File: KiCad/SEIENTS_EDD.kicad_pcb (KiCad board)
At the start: 2 copper layers, 144.1 x 110 mm, 99 parts, among them IC1 A3144EUA, J1 Conn_01x02_Pin, J201 Screw_Terminal_01x04, J3 Screw_Terminal_01x05, J4 Screw_Terminal_01x02, J7 DE9_Socket, J8 DE9_Pins, M4 Motor_DC, M5 Motor_DC, M6 Motor_DC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

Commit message: Routing V1
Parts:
- U4: footprint Package_TO_SOT_SMD:SOT-563 -> MICRO:SOT-563
- moved C304 61.0 mm to (82.7, 50.1), turned to 180 degrees
- moved C302 54.1 mm to (82.7, 55.1), turned to 180 degrees
- moved TP2 38.2 mm to (118.3, 34.0)
- moved R14 21.6 mm to (121.3, 109.5), turned to 90 degrees
- moved TP10 17.8 mm to (137.4, 82.5)
- moved C14 13.9 mm to (143.6, 77.2), turned to 90 degrees
- moved C11 13.0 mm to (148.4, 77.3), turned to 90 degrees
- moved R100 6.66 mm to (126.4, 88.4)
- moved IC1 5.25 mm to (115.7, 72.5), turned to 180 degrees
- moved R209 4.37 mm to (141.0, 111.1)
- moved R23 3.57 mm to (127.7, 68.9), turned to 180 degrees
- moved R26 1.98 mm to (120.6, 112.2)
- moved C12 1.97 mm to (191.1, 37.3)
- moved R210 1.83 mm to (115.5, 120.0), turned to 180 degrees
- moved TP4 1.74 mm to (172.7, 32.6)
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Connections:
- J201 pad 2: VBAT -> unconnected-(J201-Pin_2-Pad2)
- J7 pad 9: +5V -> unconnected-(J7-Pad9)
- J8 pad 6: +5V -> unconnected-(J8-Pad6)
- U5 pad 21: POS_IN1 -> POS_IN2
- U5 pad 22: POS_IN2 -> POS_IN1
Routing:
- net GND: track 0.00 -> 171.1 mm, vias 0 -> 128
- net MCU_SDA: track 0.00 -> 72.8 mm
- net VBAT: track 0.00 -> 70.2 mm
- net MCU_SCL: track 0.00 -> 69.6 mm
- net CINTO: track 0.00 -> 64.4 mm, vias 0 -> 3
- net +5V: track 0.00 -> 57.5 mm
- net Net-(M4--): track 0.00 -> 43.9 mm
- net HALL_OUT: track 0.00 -> 41.9 mm, vias 0 -> 1
- net Net-(M4-+): track 0.00 -> 41.7 mm, vias 0 -> 1
- net Net-(J201-Pin_1): track 0.00 -> 36.7 mm, vias 0 -> 2
- net CALEFACCIÓ: track 0.00 -> 35.9 mm
- net Net-(D2-A): track 0.00 -> 35.7 mm
- net Net-(M5--): track 0.00 -> 34.9 mm
- net Net-(C72-Pad1): track 0.00 -> 34.7 mm
- net Net-(D1-A1): track 0.00 -> 32.6 mm
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- added copper zone on F.Cu, net +3.3V
- added copper zone on F.Cu, net +5V
- added copper zone on B.Cu, net GND

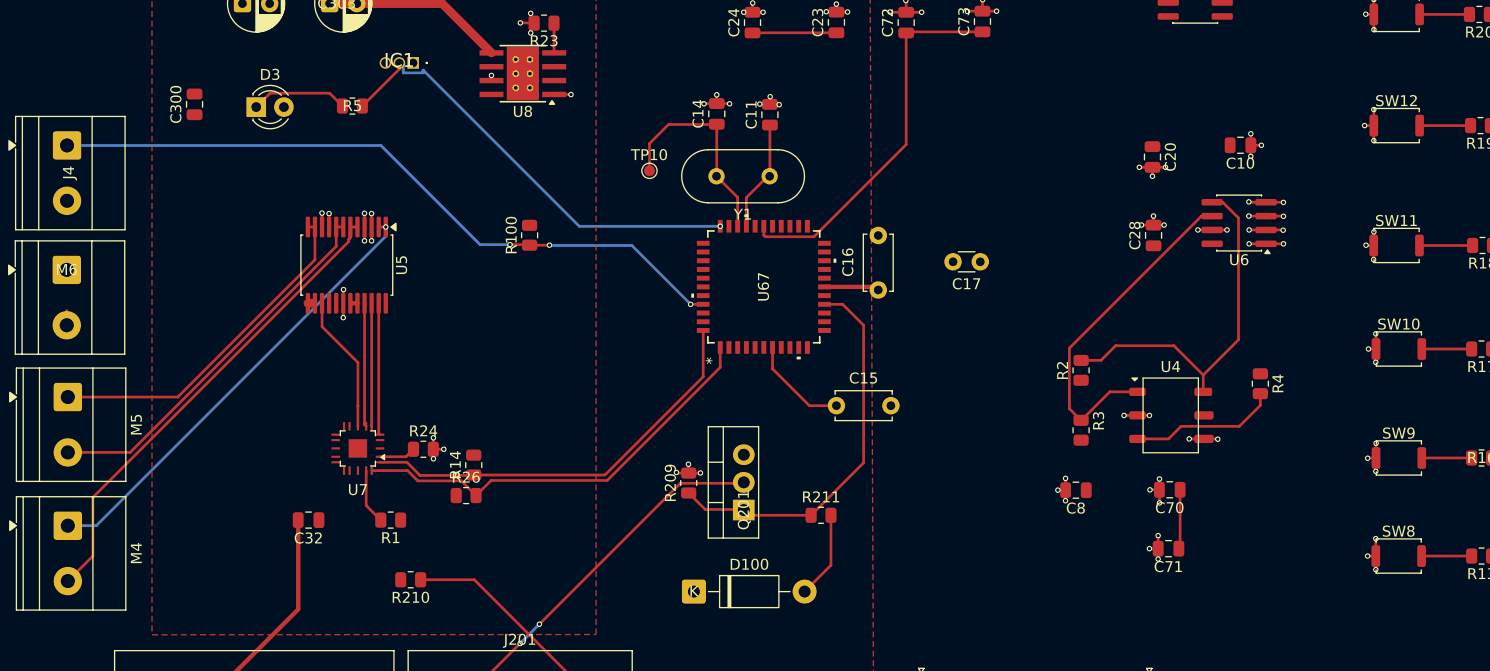
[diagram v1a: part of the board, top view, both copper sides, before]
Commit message: Modificació al routing
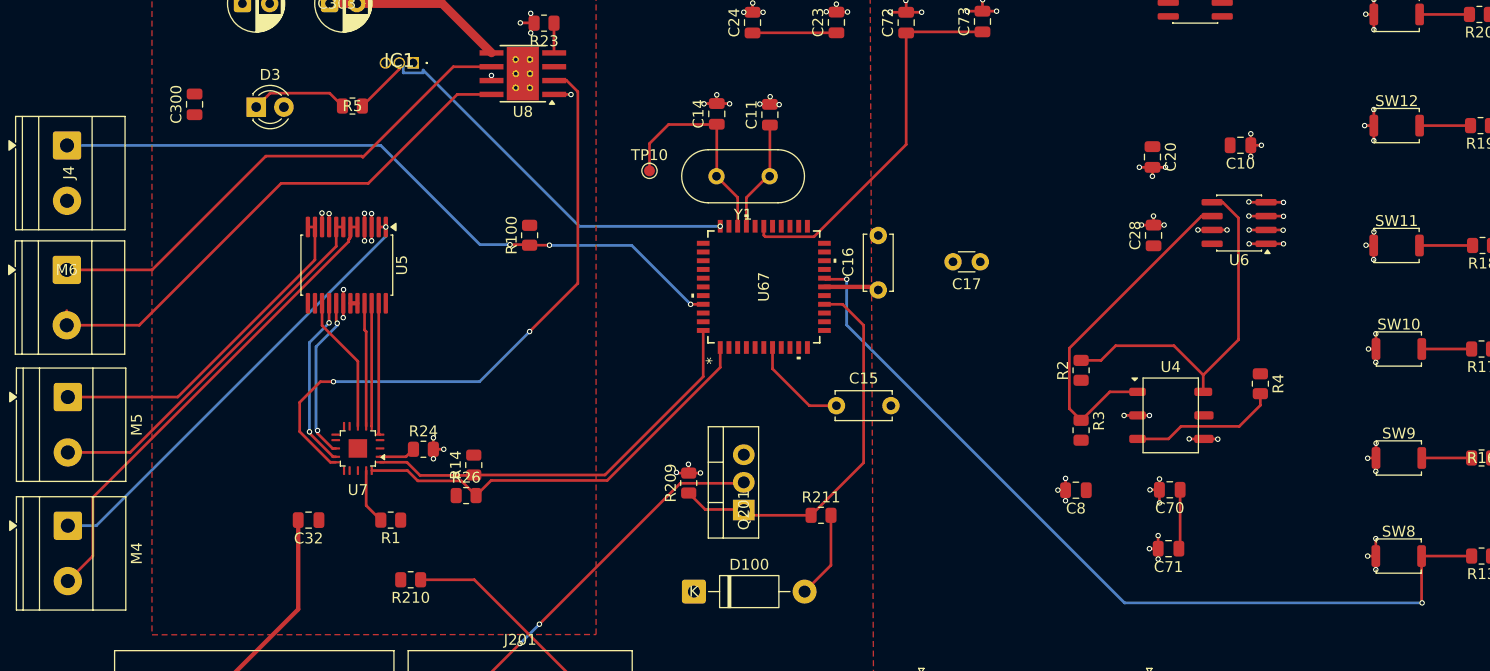
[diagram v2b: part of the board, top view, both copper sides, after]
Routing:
- net Net-(J3-Pin_1): track 4.59 -> 78.6 mm, vias 0 -> 2
- net ALT_IN2: track 0.00 -> 57.4 mm, vias 0 -> 2
- net Net-(M6--): track 1.35 -> 49.1 mm
- net Net-(M6-+): track 0.00 -> 46.8 mm
- net REC_IN2: track 0.00 -> 16.0 mm, vias 0 -> 2
- net REC_IN1: track 0.00 -> 15.1 mm, vias 0 -> 2

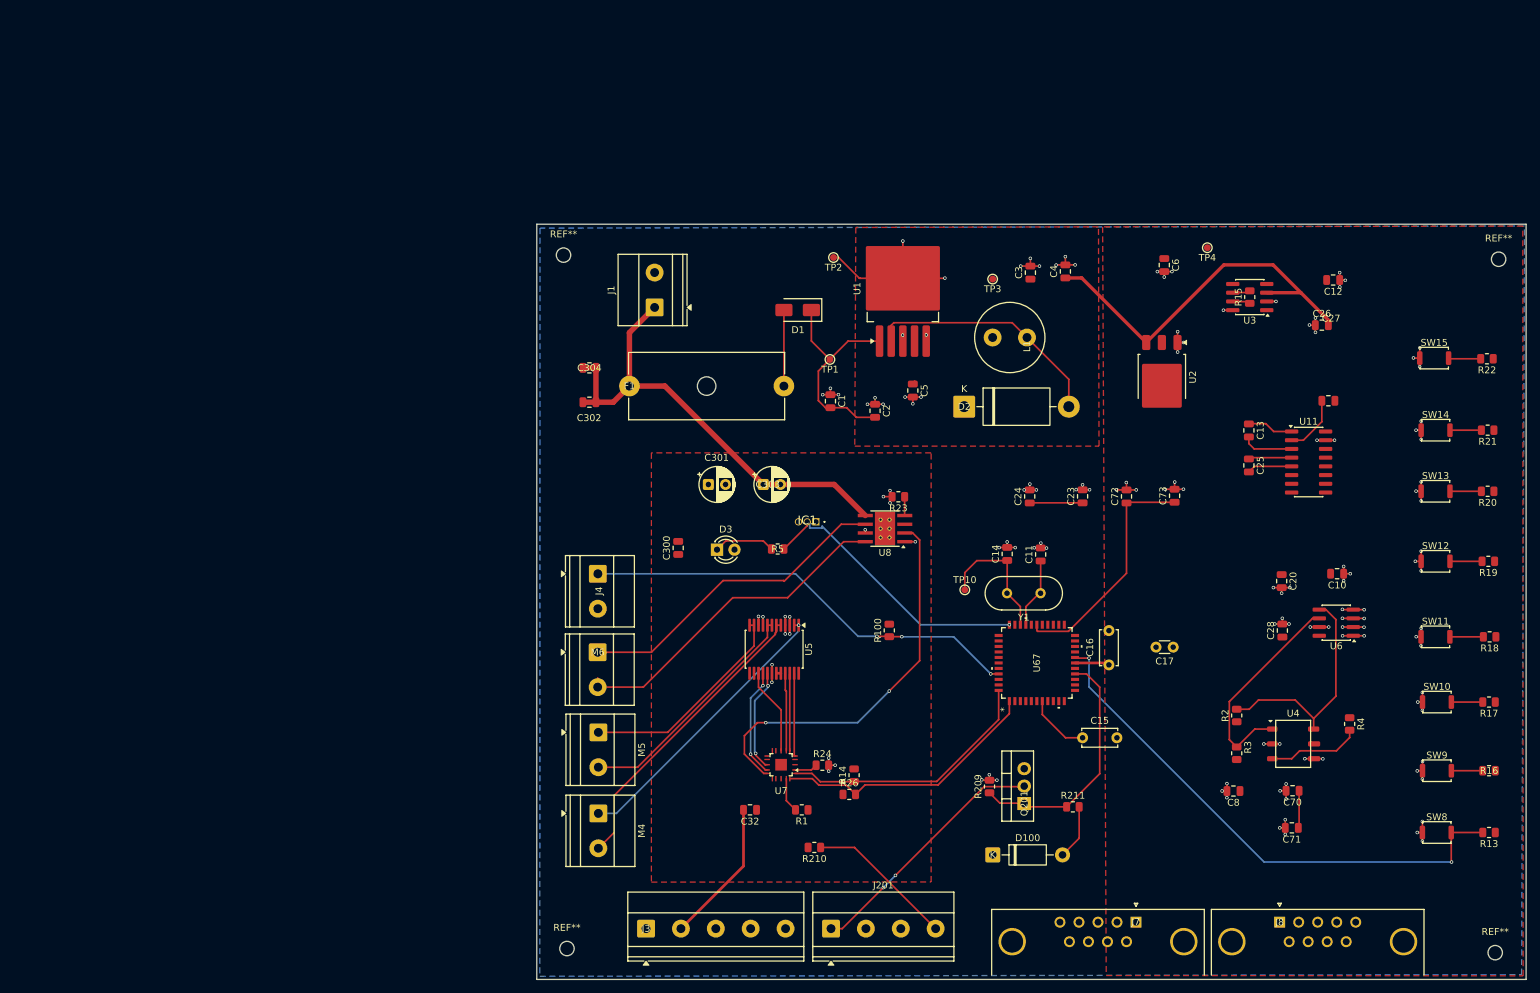
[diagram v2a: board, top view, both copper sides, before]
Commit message: Modificació al routing
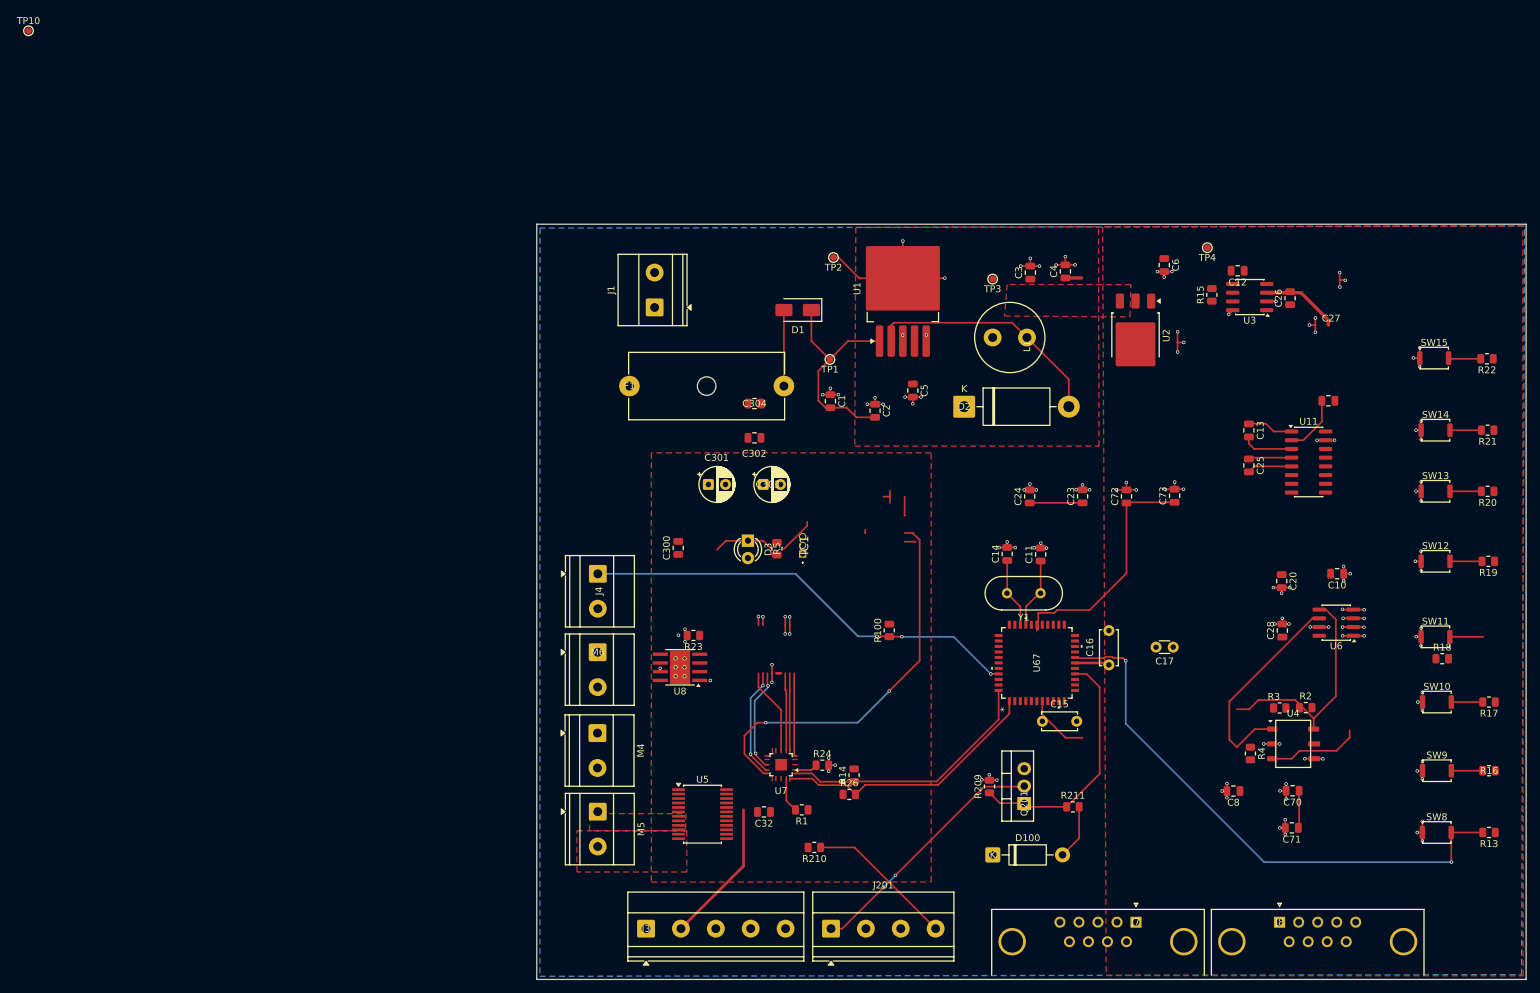
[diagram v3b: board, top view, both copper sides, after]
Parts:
- removed REF** (x4): MountingHole_2.1mm, MountingHole:MountingHole_2.1mm
- moved TP10 158.8 mm to (1.02, 1.02)
- moved U8 36.0 mm to (95.9, 93.7)
- moved R23 36.0 mm to (97.9, 89.1)
- moved U5 26.2 mm to (99.2, 115.1), turned to 0 degrees
- moved C302 24.6 mm to (106.8, 60.3)
- moved C304 24.6 mm to (106.8, 55.3)
- moved R4 15.1 mm to (179.0, 106.3)
- moved C12 14.0 mm to (177.1, 36.0)
- moved M4 11.7 mm to (83.9, 103.3)
- moved M5 11.6 mm to (83.9, 114.8)
- moved R2 10.1 mm to (187.1, 99.6), turned to 0 degrees
- moved R3 9.10 mm to (183.3, 99.7), turned to 180 degrees
- moved R18 7.60 mm to (206.9, 92.5), turned to 0 degrees
- moved U2 7.16 mm to (162.3, 45.4)
- moved C15 6.33 mm to (148.7, 101.6)
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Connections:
- C300 pad 2: +3.3V -> Net-(C300-Pad2)
- C301 pad 2: +3.3V -> Net-(C300-Pad2)
- C302 pad 1: VBAT -> VBAT/FUSE
- C302 pad 2: VBAT -> GND
- C303 pad 1: VBAT -> VBAT/FUSE
- C303 pad 2: VBAT -> GND
- C304 pad 2: VBAT -> GND
- C32 pad 2: +3.3V -> GND
- D1 pad 2: Net-(D1-A2) -> VBAT/FUSE
- F1 pad 2: Net-(D1-A2) -> VBAT/FUSE
- U5 pad 11: Net-(M5-+) -> Net-(M5--)
- U5 pad 12: Net-(M5-+) -> Net-(M5--)
- U5 pad 13: VBAT -> VBAT/FUSE
- U5 pad 14: VBAT -> VBAT/FUSE
- U5 pad 24: VBAT -> VBAT/FUSE
- U5 pad 7: Net-(M5--) -> Net-(M5-+)
- U5 pad 8: Net-(M5--) -> Net-(M5-+)
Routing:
- net VBAT: track 69.8 -> 0.00 mm
- net Net-(M6--): track 49.1 -> 0.00 mm
- net Net-(M6-+): track 46.8 -> 0.00 mm
- net Net-(M4--): track 43.9 -> 0.00 mm
- net +5V: track 57.5 -> 15.3 mm
- net HALL_OUT: track 41.9 -> 0.00 mm, vias 1 -> 0
- net Net-(M4-+): track 41.7 -> 0.00 mm, vias 1 -> 0
- net Net-(M5--): track 34.9 -> 0.00 mm
- net Net-(M5-+): track 31.6 -> 0.00 mm
- net VBAT/FUSE: track 0.00 -> 11.1 mm
- net Net-(D1-A2): track 11.1 -> 0.00 mm
- net Net-(U67-OSC2/CLKO/CN29/RA3): track 19.6 -> 10.2 mm
- net GND: track 171.1 -> 175.9 mm
- net Net-(J3-Pin_1): track 78.6 -> 81.6 mm
- net CANL: track 2.59 -> 0.04 mm
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- added copper zone on F.Cu, net Net-(M5-+)
- added copper zone on F.Cu, net Net-(M5--)

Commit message: Routing V2
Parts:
- added REF**: MountingHole_3mm, MountingHole:MountingHole_3mm, F.Cu at (79.2, 33.6)
- added REF**: MountingHole_3mm, MountingHole:MountingHole_3mm, F.Cu at (214.6, 134.6)
- added REF**: MountingHole_3mm, MountingHole:MountingHole_3mm, F.Cu at (214.1, 33.8)
- added REF**: MountingHole_3mm, MountingHole:MountingHole_3mm, F.Cu at (79.8, 134.5)
- moved R18 7.76 mm to (214.0, 89.3), turned to 180 degrees
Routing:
- net ALT_IN2: track 57.4 -> 0.50 mm, vias 2 -> 0
- net GND: track 175.9 -> 145.8 mm, vias 128 -> 111
- net +3.3V: track 26.8 -> 5.06 mm
- net REC_IN2: track 16.0 -> 0.24 mm, vias 2 -> 0
- net REC_IN1: track 15.1 -> 0.29 mm, vias 2 -> 0
- net +5V: track 15.3 -> 1.58 mm
- net Net-(U4-ALERT): track 13.6 -> 0.00 mm
- net REC_PWM: track 12.6 -> 0.00 mm
- net POS_PWM: track 12.1 -> 0.17 mm
- net POS_IN2: track 11.3 -> 0.00 mm
- net POS_IN1: track 11.3 -> 0.01 mm
- net Net-(D3-K): track 8.93 -> 0.00 mm
- net Net-(U8-ILIM): track 2.74 -> 0.00 mm
- added copper zone on B.Cu, net +3.3V
- added copper zone on B.Cu, net +5V
- added copper zone on F.Cu, net GND
- removed copper zone on F.Cu, net +3.3V
- removed copper zone on B.Cu, net GND

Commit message: Modificació al routing
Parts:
- removed REF** (x4): MountingHole_3mm, MountingHole:MountingHole_3mm
- removed TP10: TestPoint, TestPoint:TestPoint_Pad_D1.0mm
- C16: footprint Capacitor_THT:C_Disc_D5.0mm_W2.5mm_P5.00mm -> Capacitor_SMD:C_0805_2012Metric
- moved R15 84.7 mm to (147.9, 120.3)
- moved U3 84.7 mm to (153.4, 120.6)
- moved C26 84.4 mm to (161.0, 121.0)
- moved C12 82.4 mm to (155.6, 115.5)
- moved J3 78.5 mm to (148.6, 78.5), turned to -90 degrees
- moved R209 56.6 mm to (87.8, 130.2), turned to -90 degrees
- moved Q201 54.5 mm to (93.9, 129.3), turned to -90 degrees
- moved C8 35.1 mm to (142.6, 120.8), turned to -90 degrees
- moved R100 32.0 mm to (95.7, 79.2)
- moved Y1 27.6 mm to (124.8, 68.8)
- moved C11 27.6 mm to (124.8, 63.1)
- moved C14 27.6 mm to (119.9, 63.1)
- moved C17 27.0 mm to (149.2, 71.2), turned to 90 degrees
- moved C16 26.7 mm to (145.4, 70.0)
- moved SW15 23.3 mm to (224.7, 35.1)
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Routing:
- net +3.3V: track 5.06 -> 319.9 mm, vias 0 -> 4
- net RX: track 0.00 -> 99.7 mm, vias 0 -> 2
- net TX: track 0.00 -> 99.5 mm, vias 0 -> 2
- net MCU_SDA: track 72.8 -> 0.00 mm
- net MCU_SCL: track 69.6 -> 0.00 mm
- net Net-(J3-Pin_1): track 81.6 -> 15.7 mm, vias 2 -> 0
- net +5V: track 1.58 -> 60.5 mm, vias 0 -> 2
- net CALEFACCIÓ: track 35.9 -> 83.1 mm
- net ALT_IN1: track 0.00 -> 36.1 mm, vias 0 -> 2
- net CANH: track 0.04 -> 34.5 mm
- net CANL: track 0.04 -> 31.7 mm
- net Net-(M4-+): track 0.00 -> 30.7 mm
- net Net-(J201-Pin_1): track 36.7 -> 7.71 mm, vias 2 -> 0
- net Net-(M4--): track 0.00 -> 28.6 mm
- net GND: track 145.8 -> 167.7 mm
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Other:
- board size 144.1 x 110 mm -> 127.1 x 110 mm
